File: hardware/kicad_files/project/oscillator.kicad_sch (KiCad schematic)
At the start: 3 parts, among them X1 TXM12M0004252DBCEO00T

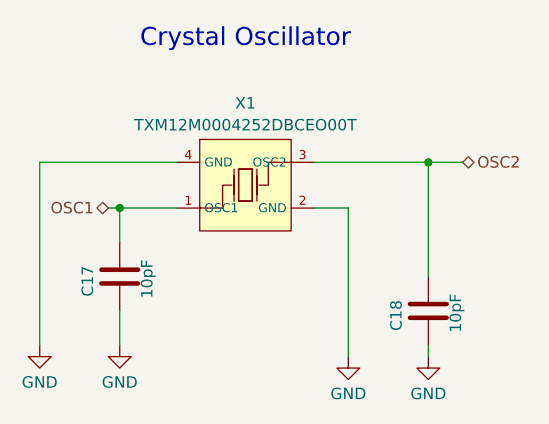
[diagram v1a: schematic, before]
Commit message: fix: replace all local symbols and footprints with versions from KiCad or project libraries
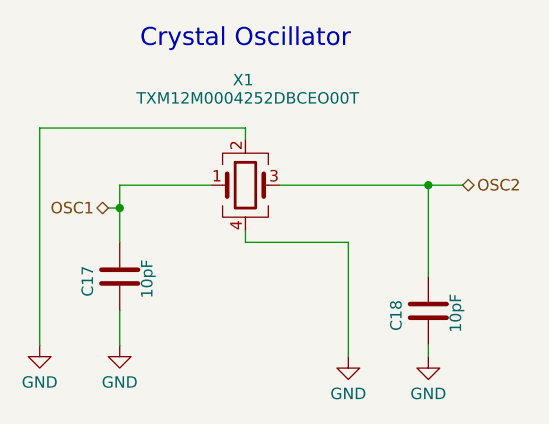
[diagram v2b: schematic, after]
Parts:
- X1: footprint easy_eda:CRYSTAL-SMD_4P-L2.5-W2.0-BL -> Crystal:Crystal_SMD_2520-4Pin_2.5x2.0mm; symbol easy_eda:TXM12M0004252DBCEO00T -> Device:Crystal_GND24
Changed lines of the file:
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@@
+	)
+	(junction
+		(at 157.48 88.9)
+		(diameter 0)
+		(color 0 0 0 0)
 	)
 	(junction
@@
 		(color 0 0 0 0)
 	)
-	(junction
-		(at 157.48 86.36)
-		(diameter 0)
-		(color 0 0 0 0)
-	)
 	(wire
 		(pts
@@
 	(wire
 		(pts
-			(xy 148.59 91.44) (xy 148.59 107.95)
-		)
-		(stroke
-			(width 0)
-			(type default)
-		)
-	)
-	(wire
-		(pts
-			(xy 114.3 86.36) (xy 114.3 106.68)
+			(xy 137.16 82.55) (xy 137.16 83.82)
+		)
+		(stroke
+			(width 0)
+			(type default)
+		)
+	)
+	(wire
+		(pts
+			(xy 114.3 82.55) (xy 114.3 106.68)
+		)
+		(stroke
+			(width 0)
+			(type default)
+		)
+	)
+	(wire
+		(pts
+			(xy 114.3 82.55) (xy 137.16 82.55)
+		)
+		(stroke
+			(width 0)
+			(type default)
+		)
+	)
+	(wire
+		(pts
+			(xy 137.16 93.98) (xy 137.16 95.25)
 		)
 		(stroke
@@
 	(wire
 		(pts
-			(xy 144.78 86.36) (xy 157.48 86.36)
+			(xy 123.19 91.44) (xy 123.19 88.9)
+		)
+		(stroke
+			(width 0)
+			(type default)
+		)
+	)
+	(wire
+		(pts
+			(xy 148.59 95.25) (xy 148.59 107.95)
+		)
+		(stroke
+			(width 0)
+			(type default)
+		)
+	)
+	(wire
+		(pts
+			(xy 140.97 88.9) (xy 157.48 88.9)
 		)
 		(stroke
@@
 	(wire
 		(pts
-			(xy 157.48 86.36) (xy 157.48 99.06)
-		)
-		(stroke
-			(width 0)
-			(type default)
-		)
-	)
-	(wire
-		(pts
-			(xy 123.19 91.44) (xy 129.54 91.44)
-		)
-		(stroke
-			(width 0)
-			(type default)
-		)
-	)
-	(wire
-		(pts
-			(xy 144.78 91.44) (xy 148.59 91.44)
-		)
-		(stroke
-			(width 0)
-			(type default)
-		)
-	)
-	(wire
-		(pts
-			(xy 157.48 86.36) (xy 161.29 86.36)
-		)
-		(stroke
-			(width 0)
-			(type default)
-		)
-	)
-	(wire
-		(pts
-			(xy 114.3 86.36) (xy 129.54 86.36)
+			(xy 157.48 88.9) (xy 157.48 99.06)
+		)
+		(stroke
+			(width 0)
+			(type default)
+		)
+	)
+	(wire
+		(pts
+			(xy 123.19 88.9) (xy 133.35 88.9)
+		)
+		(stroke
+			(width 0)
+			(type default)
+		)
+	)
+	(wire
+		(pts
+			(xy 157.48 88.9) (xy 161.29 88.9)
+		)
+		(stroke
+			(width 0)
+			(type default)
+		)
+	)
+	(wire
+		(pts
+			(xy 137.16 95.25) (xy 148.59 95.25)
 		)
 		(stroke
@@
 	(hierarchical_label "OSC2"
 		(shape bidirectional)
-		(at 161.29 86.36 0)
+		(at 161.29 88.9 0)
 		(fields_autoplaced yes)
 		(effects
@@
 		(dnp no)
 		(fields_autoplaced yes)
-		(property "Reference" "#PWR048"
+		(property "Reference" "#PWR055"
 			(at 123.19 113.03 0)
 			(effects
@@
 			(project "FABulous_board"
 				(path "/5664f05e-a3ef-4177-8026-c4580fa32c71/b4d9b251-031a-4875-8b01-0478a187070c/4c7542bb-a835-445d-b466-6e95b674eb44"
-					(reference "#PWR048")
+					(reference "#PWR055")
 					(unit 1)
 				)
@@
 	)
 	(symbol
-		(lib_id "easy_eda:TXM12M0004252DBCEO00T")
+		(lib_id "Device:Crystal_GND24")
 		(at 137.16 88.9 0)
 		(unit 1)
@@
 		(dnp no)
 		(property "Reference" "X1"
-			(at 137.16 79.8025 0)
+			(at 136.906 77.216 0)
 			(effects
 				(font
@@
 		)
 		(property "Value" "TXM12M0004252DBCEO00T"
-			(at 137.16 82.2268 0)
-			(effects
-				(font
-					(size 1.27 1.27)
-				)
-			)
-		)
-		(property "Footprint" "easy_eda:CRYSTAL-SMD_4P-L2.5-W2.0-BL"
-			(at 137.16 99.06 0)
-			(effects
-				(font
-					(size 1.27 1.27)
-					(italic yes)
-				)
-				(hide yes)
-			)
-		)
-		(property "Datasheet" "https://item.szlcsc.com/67038.html"
-			(at 134.874 88.773 0)
-			(effects
-				(font
-					(size 1.27 1.27)
-				)
-				(justify left)
-				(hide yes)
-			)
-		)
-		(property "Description" ""
+			(at 137.414 79.248 0)
+			(effects
+				(font
+					(size 1.27 1.27)
+				)
+			)
+		)
+		(property "Footprint" "Crystal:Crystal_SMD_2520-4Pin_2.5x2.0mm"
+			(at 137.16 88.9 0)
+			(effects
+				(font
+					(size 1.27 1.27)
+				)
+				(hide yes)
+			)
+		)
+		(property "Datasheet" "~"
+			(at 137.16 88.9 0)
+			(effects
+				(font
+					(size 1.27 1.27)
+				)
+				(hide yes)
+			)
+		)
+		(property "Description" "Four pin crystal, GND on pins 2 and 4"
 			(at 137.16 88.9 0)
 			(effects
@@
 		(dnp no)
 		(fields_autoplaced yes)
-		(property "Reference" "#PWR047"
+		(property "Reference" "#PWR054"
 			(at 114.3 113.03 0)
 			(effects
@@
 			(project "FABulous_board"
 				(path "/5664f05e-a3ef-4177-8026-c4580fa32c71/b4d9b251-031a-4875-8b01-0478a187070c/4c7542bb-a835-445d-b466-6e95b674eb44"
-					(reference "#PWR047")
+					(reference "#PWR054")
 					(unit 1)
 				)
@@
 		(dnp no)
 		(fields_autoplaced yes)
-		(property "Reference" "#PWR049"
+		(property "Reference" "#PWR056"
 			(at 148.59 114.3 0)
 			(effects
@@
 			(project "FABulous_board"
 				(path "/5664f05e-a3ef-4177-8026-c4580fa32c71/b4d9b251-031a-4875-8b01-0478a187070c/4c7542bb-a835-445d-b466-6e95b674eb44"
-					(reference "#PWR049")
+					(reference "#PWR056")
 					(unit 1)
 				)
@@
 		(dnp no)
 		(fields_autoplaced yes)
-		(property "Reference" "#PWR050"
+		(property "Reference" "#PWR057"
 			(at 157.48 114.3 0)
 			(effects
@@
 			(project "FABulous_board"
 				(path "/5664f05e-a3ef-4177-8026-c4580fa32c71/b4d9b251-031a-4875-8b01-0478a187070c/4c7542bb-a835-445d-b466-6e95b674eb44"
-					(reference "#PWR050")
+					(reference "#PWR057")
 					(unit 1)
 				)
